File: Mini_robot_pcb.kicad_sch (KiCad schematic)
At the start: 39 parts, among them J1 USB_B_Mini, J10 Conn_01x06_Socket, J11 Conn_01x08_Socket, J12 Conn_01x06_Socket, J2 USB_B_Micro, J3 Conn_01x04_Pin, J4 Conn_01x08_Pin, J5 Conn_01x06_Pin, J6 Moteur 2, J7 Moteur 1, J8 Power, J9 Conn_01x06_Pin, SW1 RESET BUTTON, U1 ATmega328P-A, U2 L298HN, U3 LM7805_TO220, U4 LP2985-3.3, Y1 Crystal 16MHz

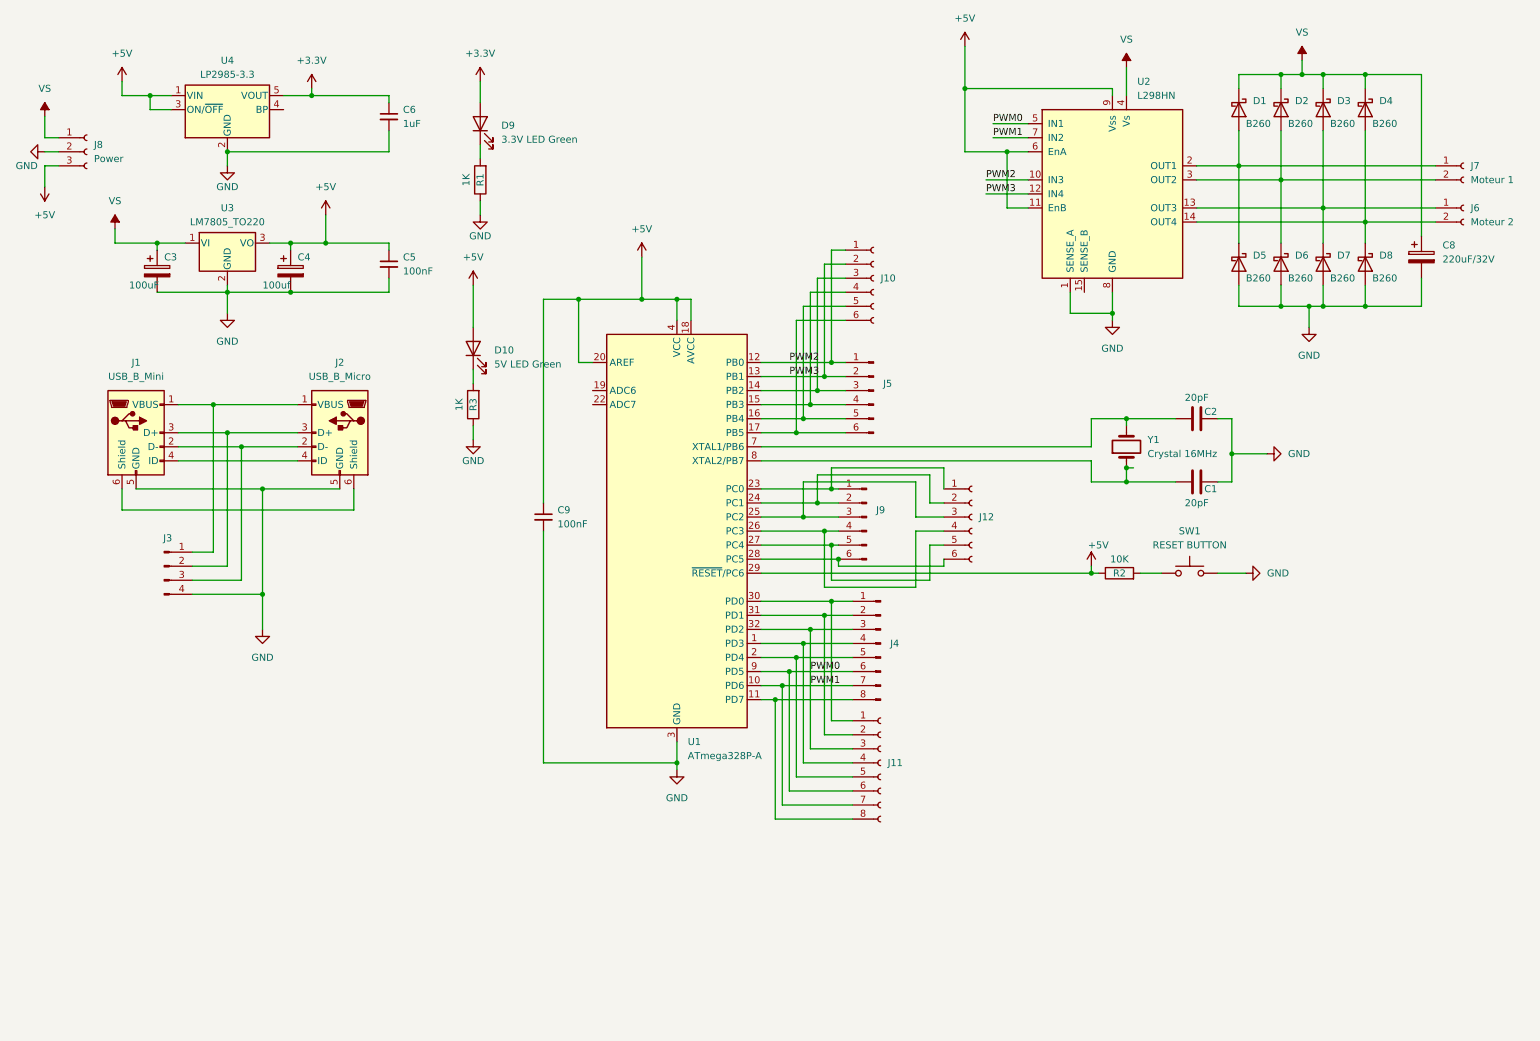
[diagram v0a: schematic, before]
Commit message: Add bleutooth and FTDI
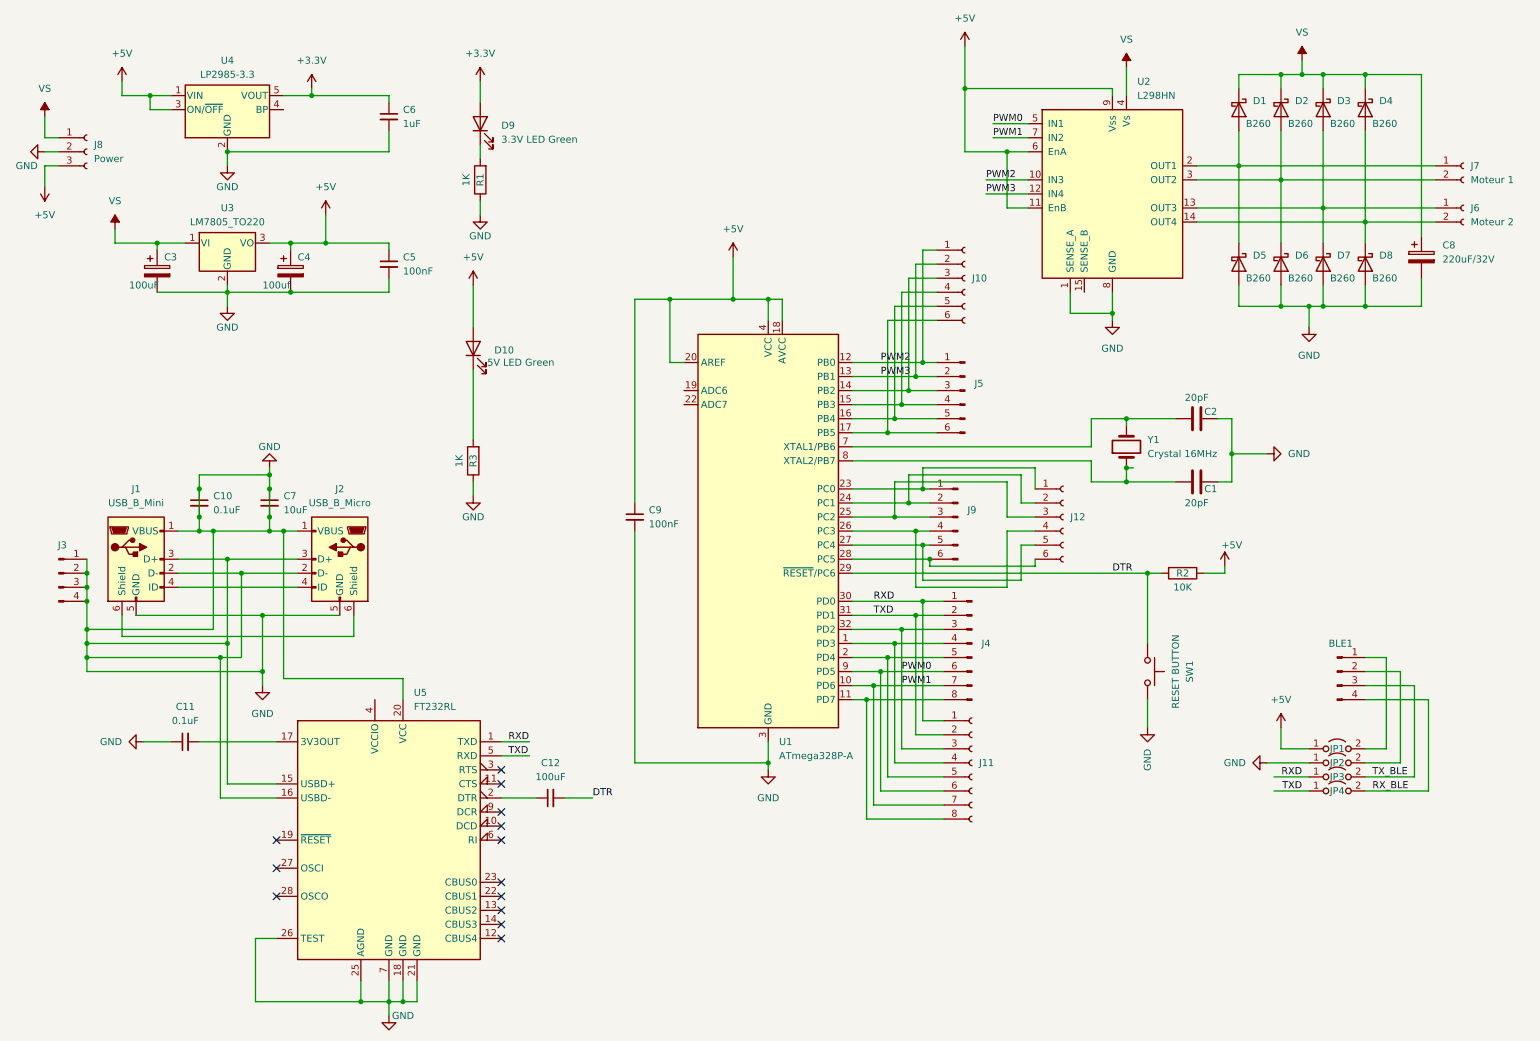
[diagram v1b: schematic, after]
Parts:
- added BLE1: Conn_01x04_Pin, Connector_PinSocket_2.54mm:PinSocket_1x04_P2.54mm_Vertical, symbol Connector:Conn_01x04_Pin
- added C10, C11: 0.1uF, Capacitor_SMD:C_0805_2012Metric_Pad1.18x1.45mm_HandSolder, symbol Device:C_Small
- added C12: 100uF, Capacitor_SMD:C_0805_2012Metric_Pad1.18x1.45mm_HandSolder, symbol Device:C_Small
- added C7: 10uF, Capacitor_SMD:C_0805_2012Metric_Pad1.18x1.45mm_HandSolder, symbol Device:C_Small
- added JP1, JP2, JP3, JP4: Jumper_2_Open, Jumper:SolderJumper-2_P1.3mm_Open_Pad1.0x1.5mm, symbol Jumper:Jumper_2_Open
- added U5: FT232RL, Package_SO:SSOP-28_5.3x10.2mm_P0.65mm, symbol Interface_USB:FT232RL
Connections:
- net +5V: now also JP1.1 (A); no longer U1.29 (~{RESET}/PC6)
- net GND: now also J1.1 (VBUS), J1.2 (D-), J1.3 (D+), J2.1 (VBUS), J2.2 (D-), J2.3 (D+), J3.1 (Pin_1), J3.2 (Pin_2), J3.3 (Pin_3), C10.1, C10.2, C11.1, C7.1, C7.2, JP2.1 (A), U5.15 (USBD+), U5.16 (USBD-), U5.18 (GND), U5.20 (VCC), U5.21 (GND), U5.25 (AGND), U5.26 (TEST), U5.7 (GND)
- net RXD: now reaches J11.1 (Pin_1), J4.1 (Pin_1), U1.30 (PD0)
- net RXD: now also JP3.1 (A), U5.1 (TXD)
- net TXD: now reaches J11.2 (Pin_2), J4.2 (Pin_2), U1.31 (PD1)
- net TXD: now also JP4.1 (A), U5.5 (RXD)
- net DTR: now reaches R2.2, SW1.1
- net DTR: now also U1.29 (~{RESET}/PC6), C12.2
- new net: C11.2, U5.17 (3V3OUT)
- new net: BLE1.1 (Pin_1), JP1.2 (B)
- new net: BLE1.2 (Pin_2), JP2.2 (B)
- new net: C12.1, U5.2 (DTR)
- new net RX_BLE: BLE1.4 (Pin_4), JP4.2 (B)
- new net TX_BLE: BLE1.3 (Pin_3), JP3.2 (B)
- no-connect marks 0 -> 13
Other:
- moved on the sheet: C9, J1, J10, J11, J12, J2, J3, J4, J5, J9, R2, R3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
